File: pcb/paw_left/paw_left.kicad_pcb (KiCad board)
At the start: 2 copper layers, 132.3 x 96.8 mm, 40 parts, among them J1 connector, J2 connector

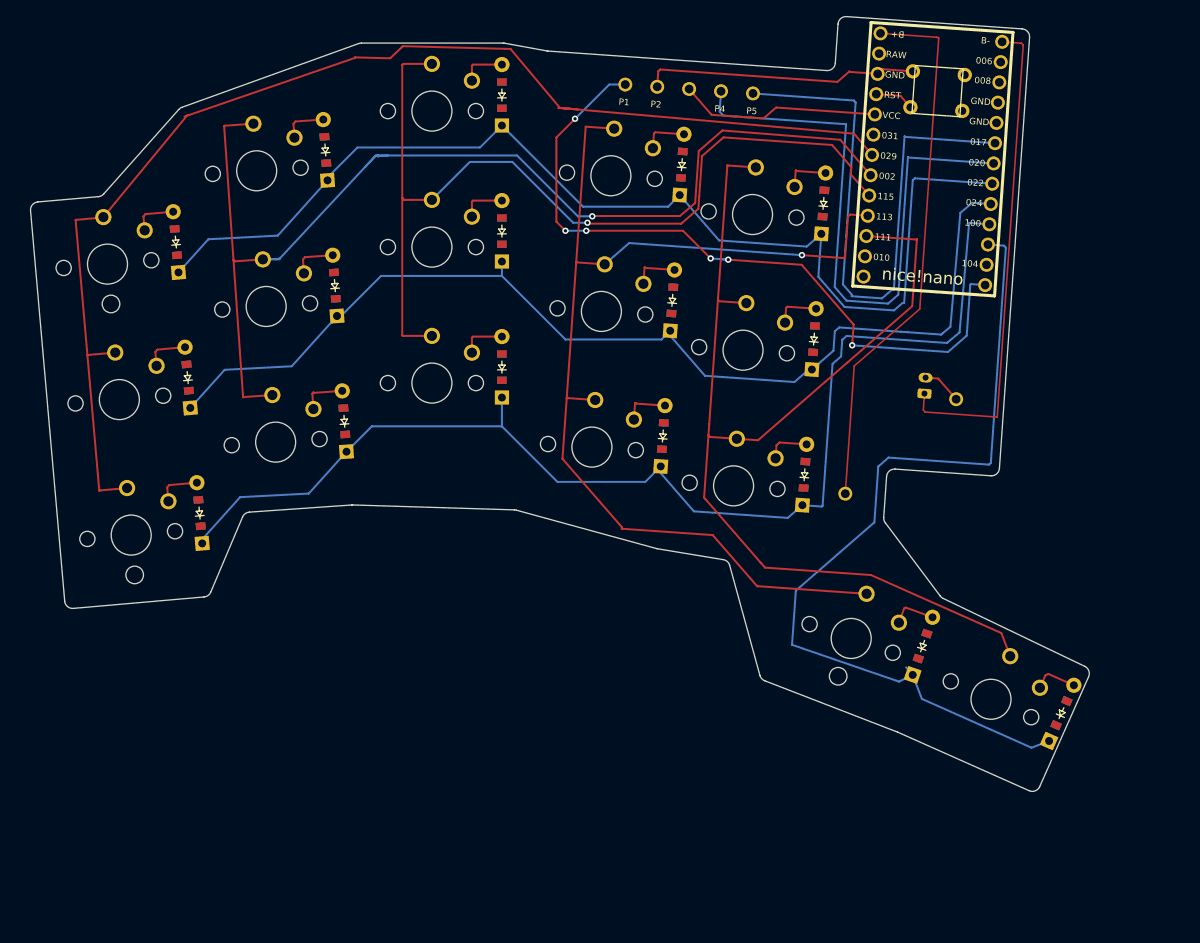
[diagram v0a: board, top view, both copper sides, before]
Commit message: Reduce stagger on middle finger by 4mm
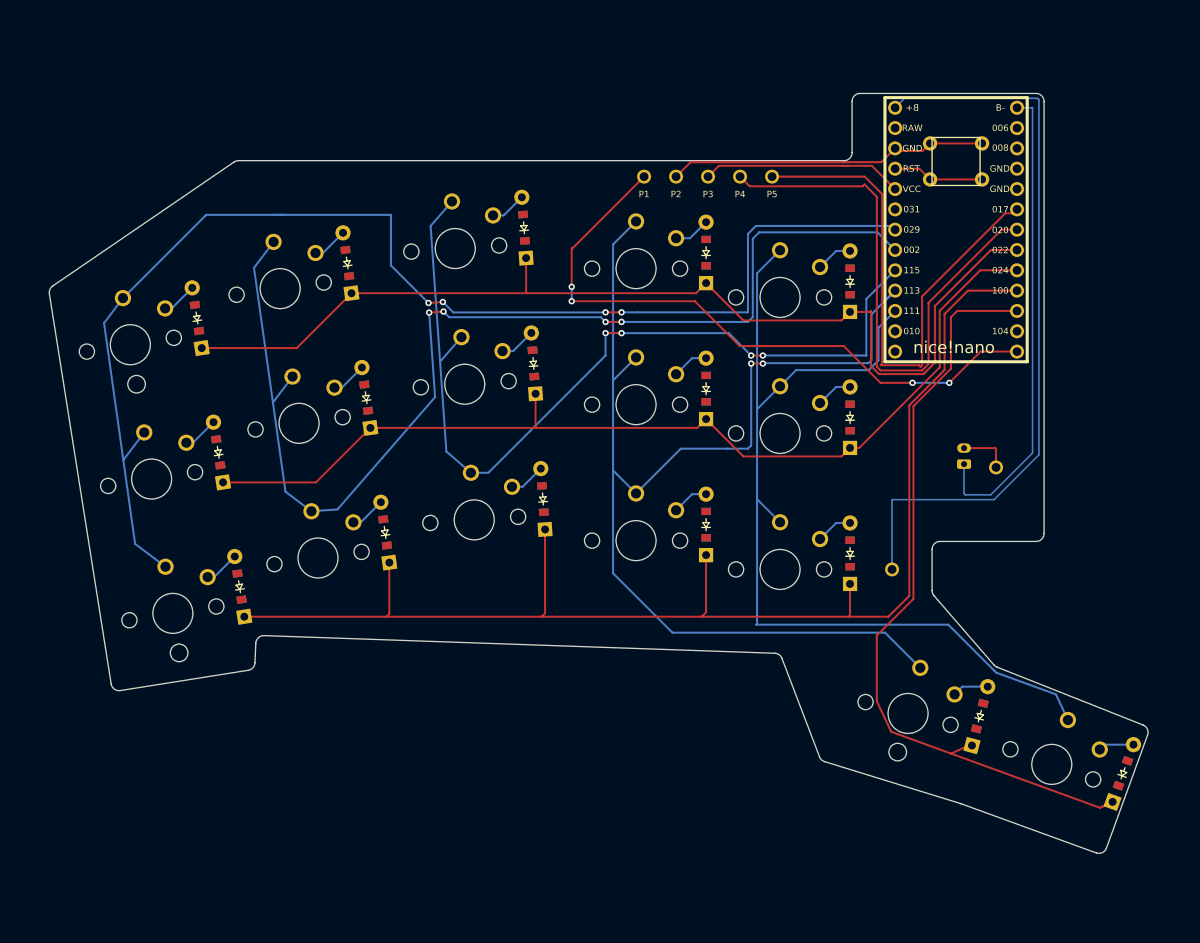
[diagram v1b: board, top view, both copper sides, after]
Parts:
- moved S7 17.9 mm to (117.0, 177.9), turned to 4 degrees
- moved S8 17.6 mm to (115.8, 161.0), turned to 4 degrees
- moved S9 17.4 mm to (114.6, 144.0), turned to 4 degrees
- moved D7 17.3 mm to (125.6, 175.3), turned to 94 degrees
- moved D8 17.0 mm to (124.4, 158.4), turned to 94 degrees
- moved D9 16.8 mm to (123.2, 141.4), turned to 94 degrees
- moved S4 15.4 mm to (97.5, 182.7), turned to 8 degrees
- moved S5 15.2 mm to (95.1, 165.9), turned to 8 degrees
- moved S6 15.0 mm to (92.7, 149.0), turned to 8 degrees
- moved D4 14.8 mm to (105.9, 179.5), turned to 98 degrees
- moved D5 14.5 mm to (103.5, 162.7), turned to 98 degrees
- moved D6 14.4 mm to (101.1, 145.8), turned to 98 degrees
- moved S10 12.9 mm to (137.2, 180.5), turned to 0 degrees
- moved S11 12.4 mm to (137.2, 163.5), turned to 0 degrees
- moved D10 12.3 mm to (146.0, 178.5), turned to 90 degrees
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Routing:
- net B+: track 68.2 -> 92.3 mm
- net P111: track 141.2 -> 120.9 mm
- net P113: track 136.3 -> 151.4 mm, vias 1 -> 2
- net P100: track 148.0 -> 161.6 mm
- net P106: track 92.0 -> 80.9 mm, vias 6 -> 4
- net P024: track 133.4 -> 122.6 mm
- net P011: track 108.6 -> 98.6 mm
- net P022: track 140.0 -> 130.0 mm
- net P020: track 76.1 -> 69.0 mm
- net P017: track 73.9 -> 67.2 mm
- net RST: track 4.93 -> 11.4 mm
- net GND: track 34.7 -> 40.2 mm
- net P029: track 158.0 -> 162.2 mm, vias 0 -> 4
- net P115: track 116.1 -> 112.3 mm, vias 1 -> 4
- net P002: track 145.3 -> 143.3 mm, vias 1 -> 4
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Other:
- board size 132.3 x 96.8 mm -> 137.3 x 95 mm

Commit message: Added pcb schema
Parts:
- removed B1: SW_Push, button_4p_65_45
- removed J1, J2: connector, connectors_1xN_th
- removed JST1: , ceoloide:battery_connector_jst_ph_2
- removed MCU1: nice_nano, nice_nano
- removed TP1: trackpad_connector, trackpad_connector_5p_th
- added Battery1: Conn_01x02_Socket, Connector_JST:JST_PH_S2B-PH-K_1x02_P2.00mm_Horizontal, B.Cu at (185.5, 174.6)
- added ONOFF1: Conn_01x01_Socket, TestPoint:TestPoint_THTPad_1.5x1.5mm_Drill0.7mm, F.Cu at (191.5, 171.6)
- added ONOFF2: Conn_01x01_Socket, TestPoint:TestPoint_THTPad_1.5x1.5mm_Drill0.7mm, F.Cu at (191.5, 175.6)
- added POGO1: Conn_01x01_Socket, TestPoint:TestPoint_THTPad_1.5x1.5mm_Drill0.7mm, F.Cu at (139.9, 135.3)
- added POGO2: Conn_01x01_Socket, TestPoint:TestPoint_THTPad_1.5x1.5mm_Drill0.7mm, F.Cu at (144.9, 135.3)
- added POGO3: Conn_01x01_Socket, TestPoint:TestPoint_THTPad_1.5x1.5mm_Drill0.7mm, F.Cu at (149.9, 135.3)
- added POGO4: Conn_01x01_Socket, TestPoint:TestPoint_THTPad_1.5x1.5mm_Drill0.7mm, F.Cu at (154.9, 135.3)
- added POGO5: Conn_01x01_Socket, TestPoint:TestPoint_THTPad_1.5x1.5mm_Drill0.7mm, F.Cu at (159.9, 135.3)
- added RESET1: Switch, Button_Switch_THT:SW_TH_Tactile_Omron_B3F-100x, F.Cu at (178.2, 132.3)
- added U1: Nice_Nano_V2, ScottoKeebs_MCU:Nice_Nano_V2, B.Cu at (181.5, 142.5)
- D1, D10, D11, D12, D13, D14, D15, D16, D17, D2, D3, D4, D5, D6, D7, D8, D9: value (none) -> Diode; footprint ComboDiode -> ScottoKeebs_Components:Diode_DO-35; moved to B.Cu
- S1, S10, S11, S12, S13, S14, S15, S16, S17, S2, S3, S4, S5, S6, S7, S8, S9: value (none) -> Keyswitch; footprint ceoloide:switch_choc_v1_v2 -> ScottoKeebs_Hotswap:Hotswap_Choc_V1V2; moved to F.Cu
- moved S5 65.1 mm to (158.1, 149.6), turned to 0 degrees
- moved D5 64.1 mm to (167.3, 156.1), turned to 90 degrees
- moved D11 61.5 mm to (91.1, 189.2), turned to 98 degrees
- moved S11 59.9 mm to (81.1, 184.3), turned to 8 degrees
- moved S4 55.6 mm to (139.9, 146.8), turned to 0 degrees
- moved D12 55.4 mm to (109.9, 186.6), turned to 98 degrees
- moved S12 51.3 mm to (99.9, 181.6), turned to 8 degrees
- moved D4 50.6 mm to (149.1, 153.3), turned to 90 degrees
- moved S3 44.9 mm to (117.3, 144.3), turned to 4 degrees
- moved D3 44.7 mm to (127.0, 150.2), turned to 94 degrees
- moved D15 42.1 mm to (167.3, 190.1)
- moved S1 39.1 mm to (76.3, 150.6), turned to 8 degrees
- moved D9 38.8 mm to (149.1, 170.3), turned to 90 degrees
- moved S13 36.0 mm to (119.7, 178.2), turned to 4 degrees
- moved D13 34.6 mm to (129.4, 184.0), turned to 94 degrees
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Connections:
- net P011 renamed Row 3
- D1 pad 1: P100 -> Row 0
- D1 pad 2: pinky_bottom -> Net-(D1-A)
- D10 pad 1: P100 -> Row 1
- D10 pad 2: index_bottom -> Net-(D10-A)
- D11 pad 1: P024 -> Row 2
- D11 pad 2: index_home -> Net-(D11-A)
- D12 pad 1: P022 -> Row 2
- D12 pad 2: index_top -> Net-(D12-A)
- D13 pad 1: P100 -> Row 2
- D13 pad 2: inner_bottom -> Net-(D13-A)
- D14 pad 1: P024 -> Row 2
- D14 pad 2: inner_home -> Net-(D14-A)
- D15 pad 1: P022 -> Row 2
- D15 pad 2: inner_top -> Net-(D15-A)
- D16 pad 2: mod1_cluster -> Net-(D16-A)
- D17 pad 2: mod2_cluster -> Net-(D17-A)
- D2 pad 1: P024 -> Row 0
- D2 pad 2: pinky_home -> Net-(D2-A)
- D3 pad 1: P022 -> Row 0
- D3 pad 2: pinky_top -> Net-(D3-A)
- D4 pad 1: P100 -> Row 0
- D4 pad 2: ring_bottom -> Net-(D4-A)
- D5 pad 1: P024 -> Row 0
- D5 pad 2: ring_home -> Net-(D5-A)
- D6 pad 1: P022 -> Row 1
- D6 pad 2: ring_top -> Net-(D6-A)
- D7 pad 1: P100 -> Row 1
- D7 pad 2: middle_bottom -> Net-(D7-A)
- D8 pad 1: P024 -> Row 1
- D8 pad 2: middle_home -> Net-(D8-A)
- D9 pad 1: P022 -> Row 1
- D9 pad 2: middle_top -> Net-(D9-A)
- S1 pad 1: pinky_bottom -> Col 0
- S1 pad 2: P029 -> Net-(D1-A)
- S10 pad 1: index_bottom -> Col 4
- S10 pad 2: P113 -> Net-(D10-A)
- S11 pad 1: index_home -> Col 0
- S11 pad 2: P113 -> Net-(D11-A)
- S12 pad 1: index_top -> Col 1
- S12 pad 2: P113 -> Net-(D12-A)
- S13 pad 1: inner_bottom -> Col 2
- S13 pad 2: P111 -> Net-(D13-A)
- S14 pad 1: inner_home -> Col 3
- S14 pad 2: P111 -> Net-(D14-A)
- S15 pad 1: inner_top -> Col 4
- S15 pad 2: P111 -> Net-(D15-A)
- S16 pad 1: mod1_cluster -> Col 3
- S16 pad 2: P113 -> Net-(D16-A)
- S17 pad 1: mod2_cluster -> Col 4
- S17 pad 2: P111 -> Net-(D17-A)
- S2 pad 1: pinky_home -> Col 1
- S2 pad 2: P029 -> Net-(D2-A)
- S3 pad 1: pinky_top -> Col 2
- S3 pad 2: P029 -> Net-(D3-A)
- S4 pad 1: ring_bottom -> Col 3
- S4 pad 2: P002 -> Net-(D4-A)
- S5 pad 1: ring_home -> Col 4
- S5 pad 2: P002 -> Net-(D5-A)
- S6 pad 1: ring_top -> Col 0
- S6 pad 2: P002 -> Net-(D6-A)
- S7 pad 1: middle_bottom -> Col 1
- S7 pad 2: P115 -> Net-(D7-A)
- S8 pad 1: middle_home -> Col 2
- S8 pad 2: P115 -> Net-(D8-A)
- S9 pad 1: middle_top -> Col 3
- S9 pad 2: P115 -> Net-(D9-A)
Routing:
- net P029: track 162.2 -> 0.00 mm, vias 4 -> 0
- net P100: track 161.6 -> 0.00 mm
- net P113: track 151.4 -> 0.00 mm, vias 2 -> 0
- net P002: track 143.3 -> 0.00 mm, vias 4 -> 0
- net P022: track 130.0 -> 0.00 mm
- net P024: track 122.6 -> 0.00 mm
- net P111: track 120.9 -> 0.00 mm
- net P115: track 112.3 -> 0.00 mm, vias 4 -> 0
- net Row 3: track 98.6 -> 0.00 mm
- net B+: track 92.3 -> 0.00 mm
- net P106: track 80.9 -> 0.00 mm, vias 4 -> 0
- net P020: track 69.0 -> 0.00 mm
- net P017: track 67.2 -> 0.00 mm
- net B-: track 59.6 -> 0.00 mm
- net GND: track 40.2 -> 0.00 mm
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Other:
- board size 137.3 x 95 mm -> 140 x 96 mm

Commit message: Added right hand PCB
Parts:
- moved RESET1 16.2 mm to (189.7, 143.8), turned to 172 degrees
- moved D17 10.3 mm to (191.9, 225.0), turned to 62 degrees
- moved S1 9.16 mm to (80.3, 142.3), turned to 0 degrees
- moved S17 8.90 mm to (186.8, 215.1), turned to -28 degrees
- moved S6 8.25 mm to (80.3, 159.3), turned to 0 degrees
- moved S11 7.97 mm to (80.3, 176.3), turned to 0 degrees
- moved D16 7.84 mm to (175.3, 216.2), turned to 67 degrees
- moved U1 7.62 mm to (185.5, 149.0), turned to 172 degrees
- moved D1 7.59 mm to (89.6, 148.8), turned to 90 degrees
- moved S2 6.98 mm to (99.3, 142.3), turned to 0 degrees
- moved D6 6.80 mm to (89.5, 165.8), turned to 90 degrees
- moved D11 6.76 mm to (89.6, 182.7), turned to 90 degrees
- moved POGO5 6.34 mm to (165.2, 138.8), turned to -8 degrees
- moved S16 6.31 mm to (169.4, 206.8), turned to -23 degrees
- moved POGO4 6.02 mm to (160.2, 138.2), turned to -8 degrees
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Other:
- board size 140 x 96 mm -> 132.4 x 102.2 mm

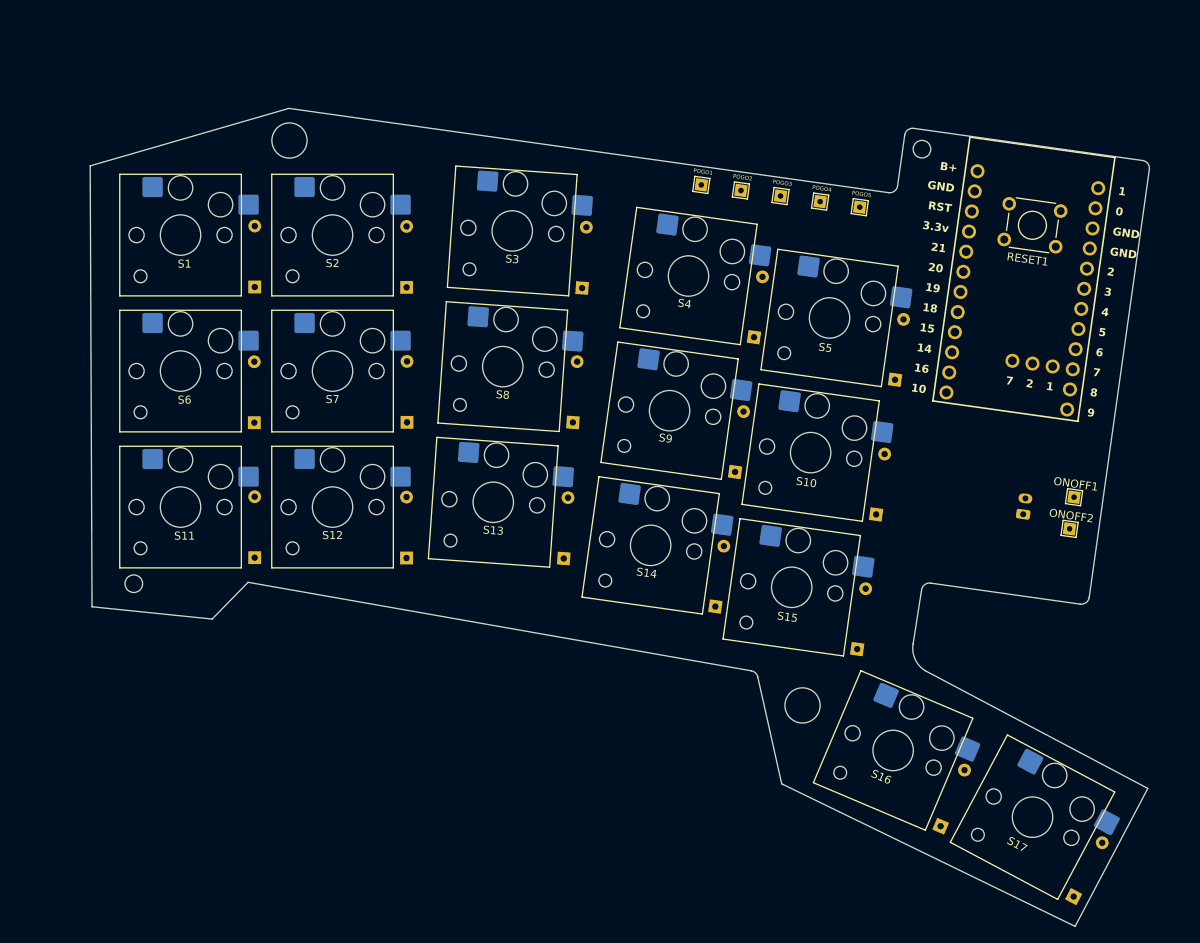
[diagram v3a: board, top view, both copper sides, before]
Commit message: Added tracks
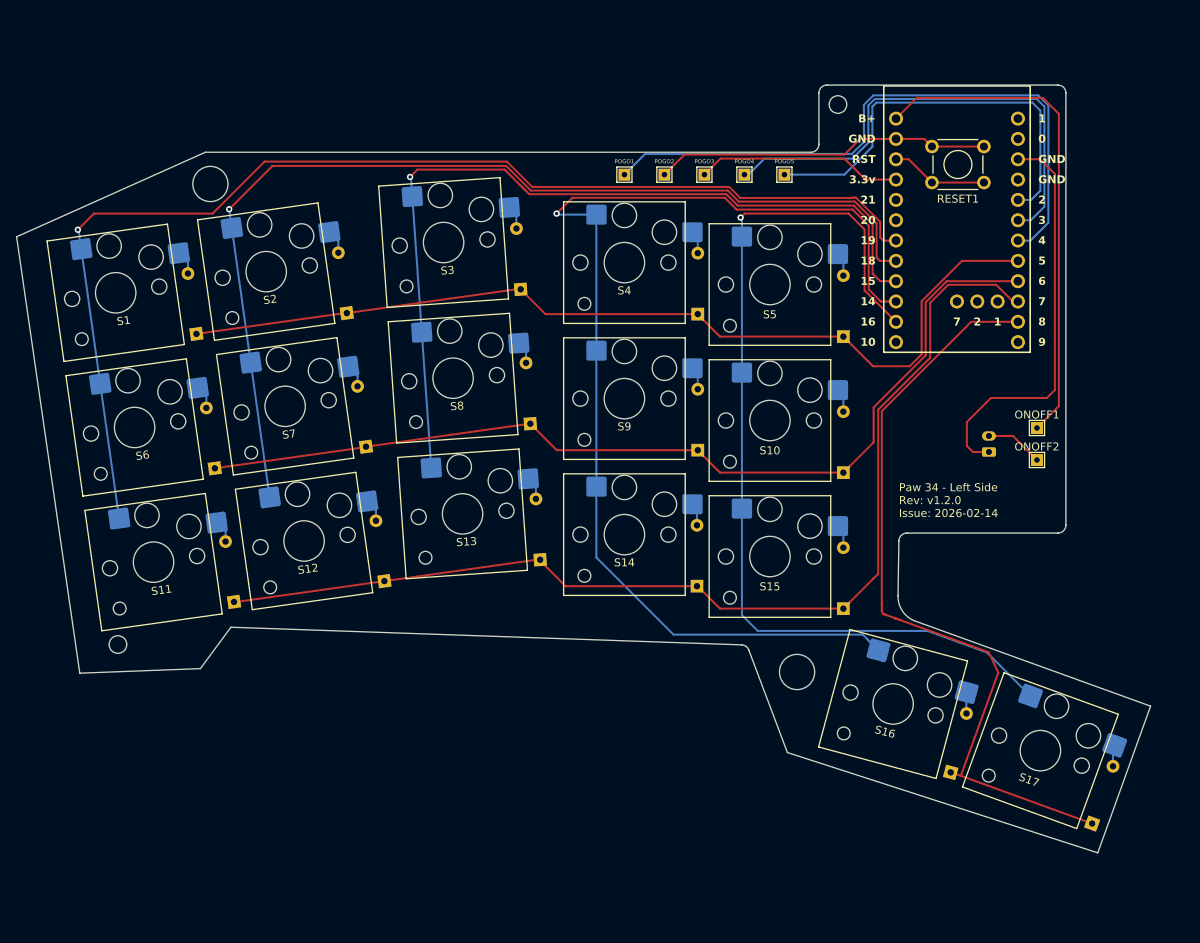
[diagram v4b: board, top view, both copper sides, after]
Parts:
- moved RESET1 12.0 mm to (180.7, 135.8), turned to 180 degrees
- moved U1 11.1 mm to (177.3, 141.5), turned to 180 degrees
- moved S1 10.9 mm to (72.2, 149.6), turned to 8 degrees
- moved POGO5 10.3 mm to (155.8, 134.8), turned to 0 degrees
- moved POGO4 10.0 mm to (150.8, 134.8), turned to 0 degrees
- moved POGO3 9.88 mm to (145.8, 134.8), turned to 0 degrees
- moved ONOFF1 9.81 mm to (187.3, 166.5), turned to 0 degrees
- moved POGO2 9.77 mm to (140.8, 134.8), turned to 0 degrees
- moved POGO1 9.70 mm to (135.8, 134.8), turned to 0 degrees
- moved ONOFF2 9.53 mm to (187.3, 170.5), turned to 0 degrees
- moved S2 9.47 mm to (91.0, 146.9), turned to 8 degrees
- moved D17 9.42 mm to (194.2, 215.9), turned to 70 degrees
- moved D1 9.35 mm to (82.3, 154.7), turned to 98 degrees
- moved S6 9.09 mm to (74.5, 166.4), turned to 8 degrees
- moved Battery1 8.88 mm to (181.3, 169.5), turned to 90 degrees
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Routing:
- net Col 0: track 0.00 -> 147.6 mm, vias 0 -> 1
- net Col 3: track 0.00 -> 143.3 mm, vias 0 -> 1
- net Row 2: track 0.00 -> 134.7 mm
- net Col 1: track 0.00 -> 129.5 mm, vias 0 -> 1
- net Col 4: track 0.00 -> 120.1 mm, vias 0 -> 1
- net Row 1: track 0.00 -> 119.7 mm
- net Row 0: track 0.00 -> 116.5 mm
- net Col 2: track 0.00 -> 107.8 mm, vias 0 -> 1
- net Row 3: track 0.00 -> 97.5 mm
- net GND: track 0.00 -> 93.3 mm
- net RDY: track 0.00 -> 79.7 mm
- net B+: track 0.00 -> 62.6 mm
- net SCL: track 0.00 -> 61.0 mm
- net SDA: track 0.00 -> 52.4 mm
- net 3V3: track 0.00 -> 25.9 mm
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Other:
- board size 132.4 x 102.2 mm -> 141.7 x 96 mm
- board text added: "Paw 34 - Left Side Rev: ${REVISION} Issue: ${ISSUE_DATE}"

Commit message: PCB rev 1.2.0
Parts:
- added G***: LOGO, MentalDesk:Paw_Logo, F.Cu at (171.8, 175.8)
